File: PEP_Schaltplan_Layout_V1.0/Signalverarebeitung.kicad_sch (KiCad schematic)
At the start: 15 parts, among them U13 LT1819, U14 LT1819, U15 LT1819

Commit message: alle_Bauteile
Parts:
- removed C28: 4.7n, Capacitor_SMD:C_1206_3216Metric, symbol ltspice:cap
- removed R36: 20k, Resistor_SMD:R_1206_3216Metric, symbol ltspice:res
- added C43, C50: 4.7n, Capacitor_SMD:C_1206_3216Metric, symbol ltspice:cap
- added C44: 470p, Capacitor_SMD:C_1206_3216Metric, symbol ltspice:cap
- added C45: 100p, Capacitor_SMD:C_1206_3216Metric, symbol ltspice:cap
- added C46, C53, C54: 47p, Capacitor_SMD:C_1206_3216Metric, symbol ltspice:cap
- added C47, C55: 22p, Capacitor_SMD:C_1206_3216Metric, symbol ltspice:cap
- added C48, C49, C56, C57: 0, Capacitor_SMD:C_1206_3216Metric, symbol ltspice:cap
- added C51: 1n, Capacitor_SMD:C_1206_3216Metric, symbol ltspice:cap
- added C52: 220p, Capacitor_SMD:C_1206_3216Metric, symbol ltspice:cap
- added R55: 1k, Resistor_SMD:R_1206_3216Metric, symbol ltspice:res
- added R56: ^0, Resistor_SMD:R_1206_3216Metric, symbol ltspice:res
- added R57, R58: 0, Resistor_SMD:R_1206_3216Metric, symbol ltspice:res
- added RV4: R_Potentiometer, Potentiometer_THT:Potentiometer_Bourns_3266Y_Vertical, symbol Device:R_Potentiometer
- added SW10, SW11, SW12, SW13, SW14, SW7, SW8, SW9: SW_DIP_x04, Button_Switch_THT:SW_DIP_SPSTx04_Slide_6.7x11.72mm_W7.62mm_P2.54mm_LowProfile, symbol Switch:SW_DIP_x04
- R35: value 10k -> 1k
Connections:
- net Rechteck: now also R57.2, R58.1; no longer R38.1, R39.2
- net Sinus: now also RV4.1
- net Sägezahn: now also SW13.5, SW13.6, SW13.7, SW13.8, SW14.5, SW14.6, SW14.7, SW14.8
- net at R35.1, U13.6 (-): now also R55.2
- net at D12.2 (-), U15.5 (+): now also R56.1, SW11.1, SW11.2, SW11.3, SW11.4, SW12.1, SW12.2, SW12.3, SW12.4; no longer R41.1
- net at R39.1, U14.6 (-): now also SW7.1, SW7.2, SW7.3, SW7.4, SW8.1, SW8.2, SW8.3, SW8.4; no longer C26.2
- net at C27.2, U14.7: now also SW10.5, SW10.6, SW10.7, SW10.8, SW9.5, SW9.6, SW9.7, SW9.8; no longer C26.1
- new net: C51.1, SW13.2
- new net: C51.2, SW11.7
- new net: C55.1, SW14.2
- new net: C55.2, SW12.7
- new net: R55.1, RV4.2
- new net: C46.1, SW10.1
- new net: C47.1, SW10.2
- new net: C48.1, SW10.3
- new net: C49.1, SW10.4
- new net: R39.2, R57.1
- new net: C43.1, SW9.2
- new net: C43.2, SW7.7
- new net: C45.1, SW9.4
- new net: C45.2, SW7.5
- new net: C56.1, SW14.3
- new net: C56.2, SW12.6
- new net: C53.2, SW11.5
- new net: C52.2, SW11.6
- new net: C50.2, SW11.8
- new net: C49.2, SW8.5
- new net: C54.1, SW14.1
- new net: C54.2, SW12.8
- new net: C44.2, SW7.6
- new net: C26.2, SW7.8
- new net: C57.2, SW12.5
- new net: C52.1, SW13.3
- new net: C50.1, SW13.1
- new net: C57.1, SW14.4
- new net: C44.1, SW9.3
- new net: C26.1, SW9.1
- new net: C46.2, SW8.8
- new net: C47.2, SW8.7
- new net: C48.2, SW8.6
- new net: R38.1, R58.2
- new net: C53.1, SW13.4
- new net: R41.1, R56.2
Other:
- moved on the sheet: C27, D12, R39, R40, R41, RV1, U14B, U15A, U15B

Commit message: Überarbeitung und Bereinigung
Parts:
- RV2: renamed from RV4; value R_Potentiometer -> 10k
- RV3: renamed from RV1; value R_Potentiometer -> 10k
- renumbered C26 to C25, C43 to C26, C44 to C27, C45 to C28, C46 to C29, C47 to C30, C48 to C31, C49 to C32, C27 to C33, C50 to C34, C51 to C35, C52 to C36, C53 to C37, C54 to C38, C55 to C39, C56 to C40, C57 to C41, D12 to D10, R35 to R20, R55 to R21, R37 to R22, R38 to R23, R58 to R24, R57 to R25, R39 to R26, R40 to R27, R41 to R28, R56 to R29, U13 to U4, U15 to U5, U14 to U6
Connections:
- net Sinus: no longer R20.2
- net +5v renamed +5V
- net -5v renamed -5V
- new net Sinus_Wien: R20.2
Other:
- moved on the sheet: C25, C26, C27, C28, C29, C30, C31, C32, C33, C34, C35, C36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

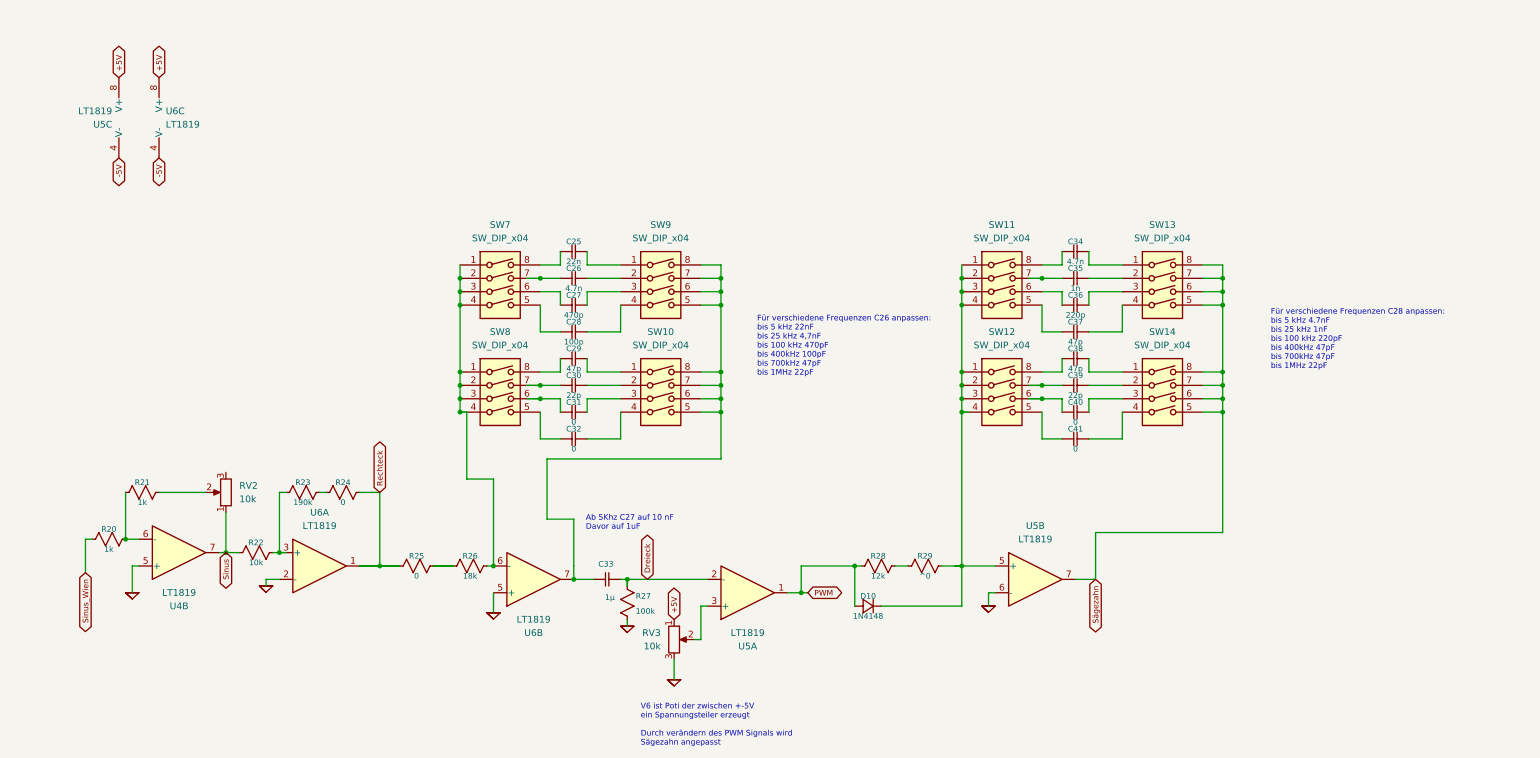
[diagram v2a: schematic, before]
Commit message: Pinheads eingefügt, GND überall (hoffentlich angebunden)
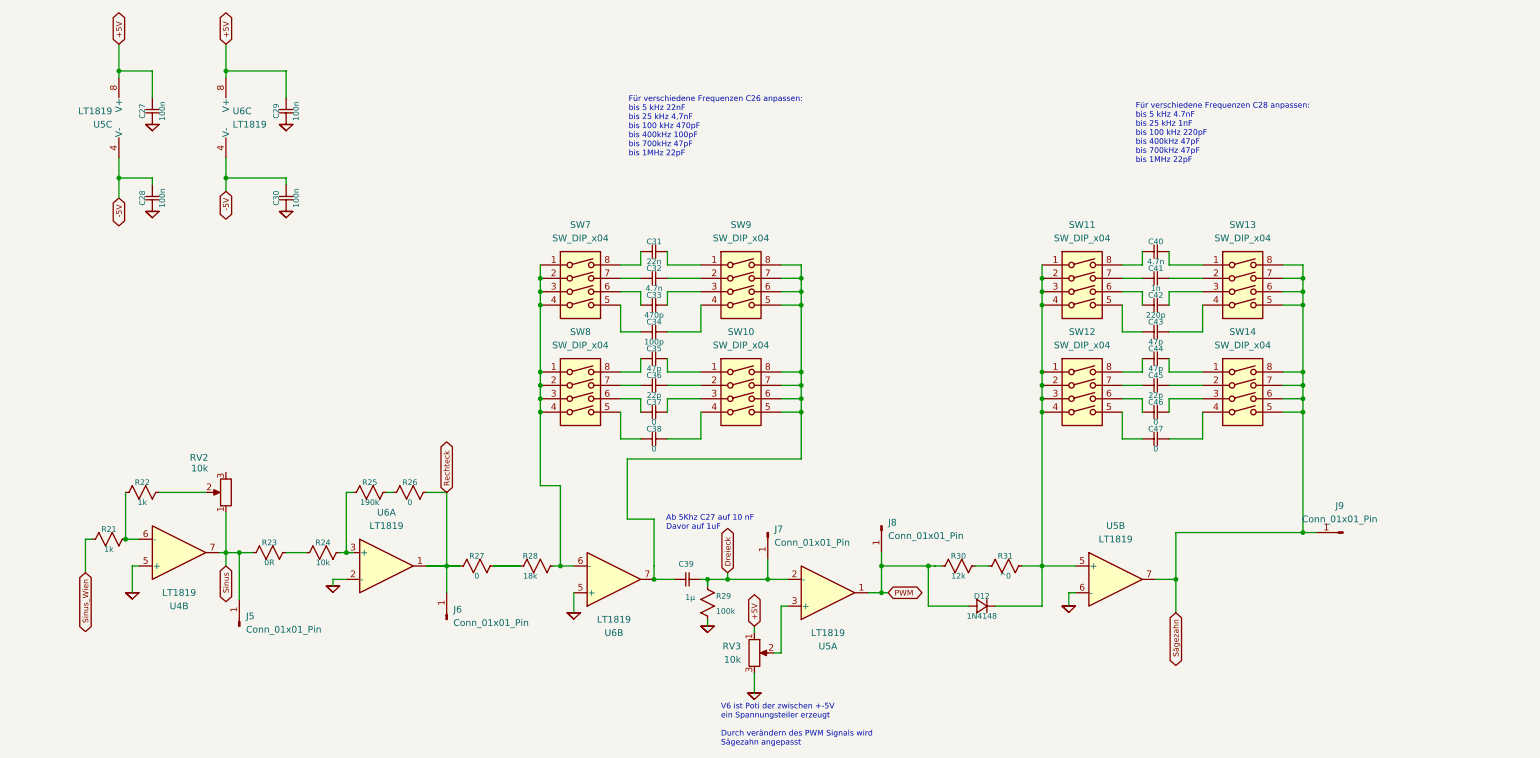
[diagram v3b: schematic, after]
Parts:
- added C27, C28, C29, C30: 100n, Capacitor_SMD:C_1206_3216Metric, symbol ltspice:cap
- added J5, J6, J7, J8, J9: Conn_01x01_Pin, Connector_PinSocket_2.54mm:PinSocket_1x01_P2.54mm_Vertical, symbol Connector:Conn_01x01_Pin
- added R23: 0R, Resistor_SMD:R_1206_3216Metric, symbol ltspice:res
- renumbered C25 to C31, C26 to C32, C27 to C33, C28 to C34, C29 to C35, C30 to C36, C31 to C37, C32 to C38, C33 to C39, C34 to C40, C35 to C41, C36 to C42, C37 to C43, C38 to C44, C39 to C45, C40 to C46, C41 to C47, D10 to D12, R20 to R21, R21 to R22, R22 to R24, R23 to R25, R24 to R26, R25 to R27, R26 to R28, R27 to R29, R28 to R30, R29 to R31
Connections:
- net +5V: now also C27.1, C29.1
- net -5V: now also C28.1, C30.1
- net 0: now also C27.2, C28.2, C29.2, C30.2
- net Dreieck: now also J7.1 (Pin_1)
- net PWM: now also J8.1 (Pin_1)
- net Rechteck: now also J6.1 (Pin_1)
- net Sinus: now also J5.1 (Pin_1), R23.2; no longer R24.2
- net Sägezahn: now also J9.1 (Pin_1)
- new net: R23.1, R24.2
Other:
- moved on the sheet: C31, C32, C33, C34, C35, C36, C37, C38, C39, C40, C41, C42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

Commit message: Widerstand eingefügt um Notfall Sinus extern, einzuspeisen
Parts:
- added R37: 0R, Resistor_SMD:R_1206_3216Metric, symbol ltspice:res
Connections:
- net Sinus_Wien: now also R37.2; no longer R21.2
- new net: R21.2, R37.1
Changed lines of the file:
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@@
 	(wire
 		(pts
+			(xy 15.24 118.11) (xy 16.51 118.11)
+		)
+		(stroke
+			(width 0)
+			(type default)
+		)
+	)
+	(wire
+		(pts
 			(xy 231.14 63.5) (xy 231.14 66.04)
 		)
@@
 	(wire
 		(pts
+			(xy 15.24 123.19) (xy 15.24 118.11)
+		)
+		(stroke
+			(width 0)
+			(type default)
+		)
+	)
+	(wire
+		(pts
 			(xy 135.89 86.36) (xy 142.24 86.36)
 		)
@@
 	(wire
 		(pts
+			(xy 22.86 118.11) (xy 25.4 118.11)
+		)
+		(stroke
+			(width 0)
+			(type default)
+		)
+	)
+	(wire
+		(pts
 			(xy 207.01 130.81) (xy 207.01 123.19)
 		)
@@
 	(wire
 		(pts
-			(xy 25.4 118.11) (xy 25.4 124.46)
-		)
-		(stroke
-			(width 0.1524)
-			(type solid)
-		)
-	)
-	(wire
-		(pts
 			(xy 127 88.9) (xy 130.81 88.9)
 		)
@@
 	(global_label "Sinus_Wien"
 		(shape bidirectional)
-		(at 25.4 124.46 270)
+		(at 15.24 123.19 270)
 		(effects
 			(font
@@
 		)
 		(property "Intersheetrefs" "${INTERSHEET_REFS}"
-			(at 25.4 124.46 0)
+			(at 15.24 123.19 0)
 			(hide yes)
 			(show_name no)
@@
 					(unit 1)
 				)
+			)
+		)
+	)
+	(symbol
+		(lib_id "ltspice:res")
+		(at 24.13 116.84 270)
+		(unit 1)
+		(body_style 1)
+		(exclude_from_sim no)
+		(in_bom yes)
+		(on_board yes)
+		(in_pos_files yes)
+		(dnp no)
+		(property "Reference" "R37"
+			(at 19.685 116.84 90)
+			(show_name no)
+			(do_not_autoplace no)
+			(effects
+				(font
+					(size 1.0668 1.0668)
+				)
+				(justify bottom)
+			)
+		)
+		(property "Value" "0R"
+			(at 19.685 119.38 90)
+			(show_name no)
+			(do_not_autoplace no)
+			(effects
+				(font
+					(size 1.0668 1.0668)
+				)
+				(justify top)
+			)
+		)
+		(property "Footprint" "Resistor_SMD:R_1206_3216Metric"
+			(at 24.13 116.84 0)
+			(hide yes)
+			(show_name no)
+			(do_not_autoplace no)
+			(effects
+				(font
+					(size 1.27 1.27)
+				)
+			)
+		)
+		(property "Datasheet" ""
+			(at 24.13 116.84 0)
+			(hide yes)
+			(show_name no)
+			(do_not_autoplace no)
+			(effects
+				(font
+					(size 1.27 1.27)
+				)
+			)
+		)
+		(property "Description" ""
+			(at 24.13 116.84 0)
+			(hide yes)
+			(show_name no)
+			(do_not_autoplace no)
+			(effects
+				(font
+					(size 1.27 1.27)
+				)
+			)
+		)
+		(property "Sim.Device" "R"
+			(at 24.13 116.84 0)
+			(hide yes)
+			(show_name no)
+			(do_not_autoplace no)
+			(effects
+				(font
+					(size 1.27 1.27)
+				)
+			)
+		)
+		(property "Sim.Params" "R=${VALUE}"
+			(at 24.13 116.84 0)
+			(hide yes)
+			(show_name no)
+			(do_not_autoplace no)
+			(effects
+				(font
+					(size 1.27 1.27)
+				)
+			)
+		)
+		(pin "2"
+		)
+		(pin "1"
+		)
+		(instances
+			(project "PEP_Schaltplan_Layout_V1.0"
+				(path "/c92bfc19-22ce-4924-9f32-1487b4215208/266255db-b3d9-42a5-82a9-1ba71b36126a"
+					(reference "R37")
+					(unit 1)
+				)

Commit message: Hab den Pin zum einspeisen vergessen
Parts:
- added J12: Conn_01x01_Pin, Connector_PinSocket_2.54mm:PinSocket_1x01_P2.54mm_Vertical, symbol Connector:Conn_01x01_Pin
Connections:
- net at R21.2, R37.1: now also J12.1 (Pin_1)
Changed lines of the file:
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@@
 	)
 	(junction
+		(at 25.4 118.11)
+		(diameter 0)
+		(color 0 0 0 0)
+	)
+	(junction
 		(at 207.01 73.66)
 		(diameter 0)
@@
 	(wire
 		(pts
+			(xy 25.4 118.11) (xy 25.4 124.46)
+		)
+		(stroke
+			(width 0)
+			(type default)
+		)
+	)
+	(wire
+		(pts
 			(xy 118.11 132.08) (xy 118.11 128.27)
 		)
@@
 					(unit 1)
 				)
+			)
+		)
+	)
+	(symbol
+		(lib_id "Connector:Conn_01x01_Pin")
+		(at 25.4 129.54 90)
+		(unit 1)
+		(body_style 1)
+		(exclude_from_sim no)
+		(in_bom yes)
+		(on_board yes)
+		(in_pos_files yes)
+		(dnp no)
+		(fields_autoplaced yes)
+		(property "Reference" "J12"
+			(at 26.67 127.6349 90)
+			(show_name no)
+			(do_not_autoplace no)
+			(effects
+				(font
+					(size 1.27 1.27)
+				)
+				(justify right)
+			)
+		)
+		(property "Value" "Conn_01x01_Pin"
+			(at 26.67 130.1749 90)
+			(show_name no)
+			(do_not_autoplace no)
+			(effects
+				(font
+					(size 1.27 1.27)
+				)
+				(justify right)
+			)
+		)
+		(property "Footprint" "Connector_PinSocket_2.54mm:PinSocket_1x01_P2.54mm_Vertical"
+			(at 25.4 129.54 0)
+			(hide yes)
+			(show_name no)
+			(do_not_autoplace no)
+			(effects
+				(font
+					(size 1.27 1.27)
+				)
+			)
+		)
+		(property "Datasheet" ""
+			(at 25.4 129.54 0)
+			(hide yes)
+			(show_name no)
+			(do_not_autoplace no)
+			(effects
+				(font
+					(size 1.27 1.27)
+				)
+			)
+		)
+		(property "Description" "Generic connector, single row, 01x01, script generated"
+			(at 25.4 129.54 0)
+			(hide yes)
+			(show_name no)
+			(do_not_autoplace no)
+			(effects
+				(font
+					(size 1.27 1.27)
+				)
+			)
+		)
+		(pin "1"
+		)
+		(instances
+			(project "PEP_Schaltplan_Layout_V1.0"
+				(path "/c92bfc19-22ce-4924-9f32-1487b4215208/266255db-b3d9-42a5-82a9-1ba71b36126a"
+					(reference "J12")
+					(unit 1)
+				)

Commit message: Leiterplatten größe definiert und erstes Auto Routing
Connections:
- net 0 renamed GND
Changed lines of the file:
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@@
 		(at 34.29 128.27 0)
 		(unit 1)
-		(body_style 0)
+		(body_style 1)
 		(exclude_from_sim no)
 		(in_bom yes)
@@
 			)
 		)
-		(property "Value" "0"
+		(property "Value" "GND"
 			(at 34.29 128.27 0)
 			(hide yes)
@@
 		(at 152.4 147.32 0)
 		(unit 1)
-		(body_style 0)
+		(body_style 1)
 		(exclude_from_sim no)
 		(in_bom yes)
@@
 			)
 		)
-		(property "Value" "0"
+		(property "Value" "GND"
 			(at 152.4 147.32 0)
 			(hide yes)
@@
 		(at 118.11 132.08 0)
 		(unit 1)
-		(body_style 0)
+		(body_style 1)
 		(exclude_from_sim no)
 		(in_bom yes)
@@
 			)
 		)
-		(property "Value" "0"
+		(property "Value" "GND"
 			(at 118.11 132.08 0)
 			(hide yes)
@@
 		(at 38.1 55.88 0)
 		(unit 1)
-		(body_style 0)
+		(body_style 1)
 		(exclude_from_sim no)
 		(in_bom yes)
@@
 			)
 		)
-		(property "Value" "0"
+		(property "Value" "GND"
 			(at 38.1 55.88 0)
 			(hide yes)
@@
 		(at 38.1 39.37 0)
 		(unit 1)
-		(body_style 0)
+		(body_style 1)
 		(exclude_from_sim no)
 		(in_bom yes)
@@
 			)
 		)
-		(property "Value" "0"
+		(property "Value" "GND"
 			(at 38.1 39.37 0)
 			(hide yes)
@@
 		(at 63.5 39.37 0)
 		(unit 1)
-		(body_style 0)
+		(body_style 1)
 		(exclude_from_sim no)
 		(in_bom yes)
@@
 			)
 		)
-		(property "Value" "0"
+		(property "Value" "GND"
 			(at 63.5 39.37 0)
 			(hide yes)
@@
 		(at 212.09 130.81 0)
 		(unit 1)
-		(body_style 0)
+		(body_style 1)
 		(exclude_from_sim no)
 		(in_bom yes)
@@
 			)
 		)
-		(property "Value" "0"
+		(property "Value" "GND"
 			(at 212.09 130.81 0)
 			(hide yes)
@@
 		(at 72.39 127 0)
 		(unit 1)
-		(body_style 0)
+		(body_style 1)
 		(exclude_from_sim no)
 		(in_bom yes)
@@
 			)
 		)
-		(property "Value" "0"
+		(property "Value" "GND"
 			(at 72.39 127 0)
 			(hide yes)
@@
 		(at 63.5 55.88 0)
 		(unit 1)
-		(body_style 0)
+		(body_style 1)
 		(exclude_from_sim no)
 		(in_bom yes)
@@
 			)
 		)
-		(property "Value" "0"
+		(property "Value" "GND"
 			(at 63.5 55.88 0)
 			(hide yes)
@@
 		(at 143.51 134.62 0)
 		(unit 1)
-		(body_style 0)
+		(body_style 1)
 		(exclude_from_sim no)
 		(in_bom yes)
@@
 			)
 		)
-		(property "Value" "0"
+		(property "Value" "GND"
 			(at 143.51 134.62 0)
 			(hide yes)

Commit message: Anpassung
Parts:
- C41: value 1n -> 2.2n
- C42: value 220p -> 1n
- C43: value 47p -> 270p
- C44: value 47p -> 120p
- C45: value 22p -> 47p
- C46: value 0 -> 22p
- C47: value 0 -> 12p
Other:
- note added: "Für verschiedene Frequenzen C28 anpassen: bis 5 kHz 4.7nF bis 25 kHz 1nF bis 100 kHz 270pF bis 400kHz 120pF bis 700kHz 47pF bis 1MHz 22pF 12pF"
- note removed: "Für verschiedene Frequenzen C28 anpassen: bis 5 kHz 4.7nF bis 25 kHz 1nF bis 100 kHz 220pF bis 400kHz 47pF bis 700kHz 47pF bis 1MHz 22pF"
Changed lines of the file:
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@@
 		)
 	)
-	(text "Für verschiedene Frequenzen C28 anpassen:\nbis 5 kHz 4.7nF\nbis 25 kHz 1nF\nbis 100 kHz 220pF\nbis 400kHz 47pF\nbis 700kHz 47pF\nbis 1MHz 22pF"
+	(text "Für verschiedene Frequenzen C28 anpassen:\nbis 5 kHz 4.7nF\nbis 25 kHz 1nF\nbis 100 kHz 270pF\nbis 400kHz 120pF\nbis 700kHz 47pF\nbis 1MHz 22pF\n12pF\n"
 		(exclude_from_sim no)
 		(at 224.79 35.306 0)
@@
 			)
 		)
-		(property "Value" "1n"
+		(property "Value" "2.2n"
 			(at 228.6 69.85 90)
 			(show_name no)
@@
 			)
 		)
-		(property "Value" "22p"
+		(property "Value" "47p"
 			(at 228.6 90.17 90)
 			(show_name no)
@@
 			)
 		)
-		(property "Value" "0"
+		(property "Value" "22p"
 			(at 228.6 95.25 90)
 			(show_name no)
@@
 			)
 		)
-		(property "Value" "47p"
+		(property "Value" "120p"
 			(at 228.6 85.09 90)
 			(show_name no)
@@
 			)
 		)
-		(property "Value" "220p"
+		(property "Value" "1n"
 			(at 228.6 74.93 90)
 			(show_name no)
@@
 			)
 		)
-		(property "Value" "0"
+		(property "Value" "12p"
 			(at 228.6 100.33 90)
 			(show_name no)
@@
 			)
 		)
-		(property "Value" "47p"
+		(property "Value" "270p"
 			(at 228.6 80.01 90)
 			(show_name no)

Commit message: Fertig
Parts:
- C31: value 22n -> 4.7n
- C32: value 4.7n -> 2.2n
- C33: value 470p -> 1n
- C34: value 100p -> 270p
- C35: value 47p -> 120p
- C36: value 22p -> 47p
- C37: value 0 -> 22p
- C38: value 0 -> 12p
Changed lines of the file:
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@@
 			)
 		)
-		(property "Value" "4.7n"
+		(property "Value" "2.2n"
 			(at 133.35 69.85 90)
 			(show_name no)
@@
 			)
 		)
-		(property "Value" "100p"
+		(property "Value" "270p"
 			(at 133.35 80.01 90)
 			(show_name no)
@@
 			)
 		)
-		(property "Value" "0"
+		(property "Value" "12p"
 			(at 133.35 100.33 90)
 			(show_name no)
@@
 			)
 		)
-		(property "Value" "470p"
+		(property "Value" "1n"
 			(at 133.35 74.93 90)
 			(show_name no)
@@
 			)
 		)
-		(property "Value" "47p"
+		(property "Value" "120p"
 			(at 133.35 85.09 90)
 			(show_name no)
@@
 			)
 		)
-		(property "Value" "22p"
+		(property "Value" "47p"
 			(at 133.35 90.17 90)
 			(show_name no)
@@
 			)
 		)
-		(property "Value" "0"
+		(property "Value" "22p"
 			(at 133.35 95.25 90)
 			(show_name no)
@@
 			)
 		)
-		(property "Value" "22n"
+		(property "Value" "4.7n"
 			(at 133.35 64.77 90)
 			(show_name no)
